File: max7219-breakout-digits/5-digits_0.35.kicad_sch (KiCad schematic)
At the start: 3 parts, among them J1 Conn_02x08_Odd_Even, U1 HDSM-443B_7-Segment_2_Digit, U2 HDSM-443B_7-Segment_3_Digit

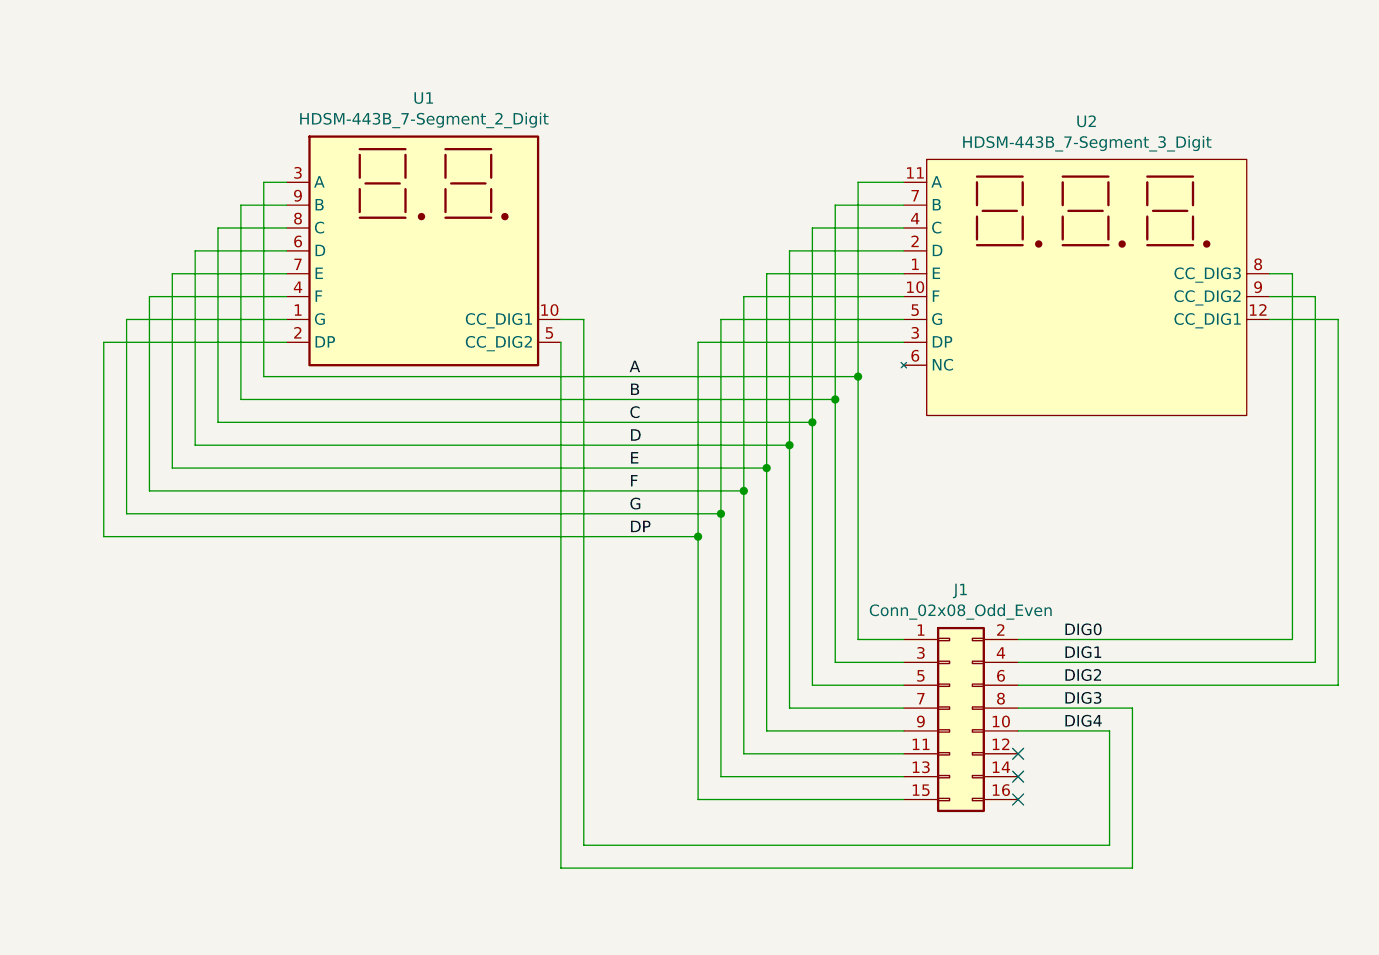
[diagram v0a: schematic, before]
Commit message: rotate IDC on 0.28 displays, plated mounting holes for 0.35 displays, set version for 0.35 displays
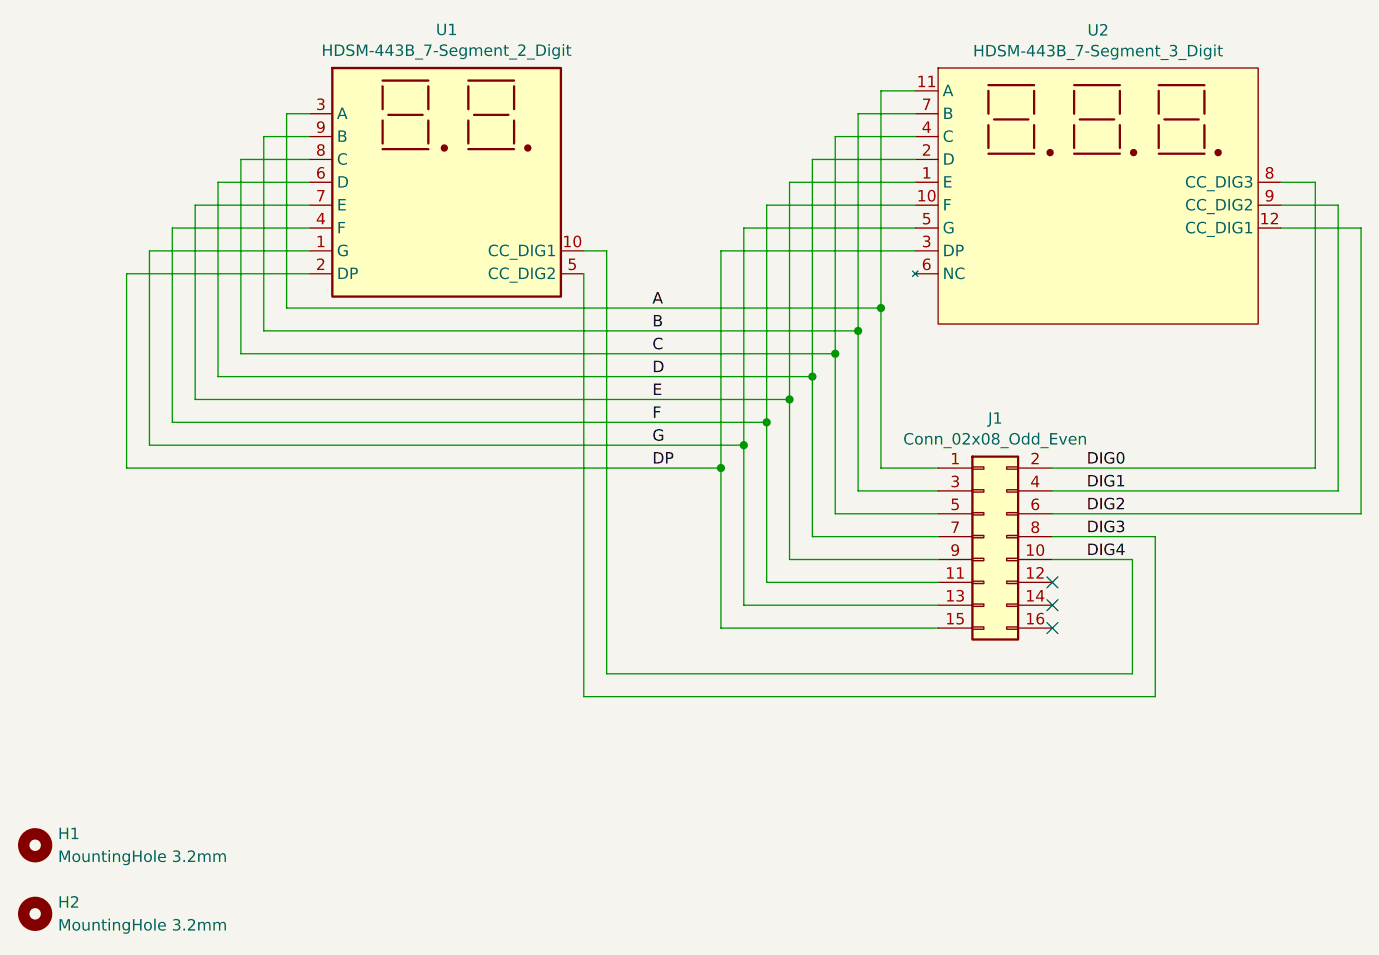
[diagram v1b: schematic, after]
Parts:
- added H1, H2: MountingHole 3.2mm, MountingHole:MountingHole_3.2mm_M3_Pad, symbol MobiFlight:MountingHole 3.2mm
- U1: footprint Display_7Segment:SN42056STH -> MobiFlight:STH_7_2 Digits_0.35_CC; symbol Display_Character:HDSM-443B_7-Segment_2_Digit -> MobiFlight:7Segment 2 digit 0.35 common cathode STH
- U2: footprint Display_7Segment:SP42056STH -> MobiFlight:STH_7_3 Digits_0.35_CC; symbol Display_Character:HDSM-443B_7-Segment_3_Digit -> MobiFlight:7Segment 3 digit 0.35 common cathode STH
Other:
- company: (none) -> MobiFlight
- title: 7 Segment 5 Digits -> 7-Segment Display Module 0.35, 5 Digits
- moved on the sheet: J1, U1, U2
